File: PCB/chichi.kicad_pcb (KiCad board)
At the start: 2 copper layers, 59 x 53 mm, 6 parts, among them U1 ESP32-C3_SUPERMINI_TH, U2 Charger_Module

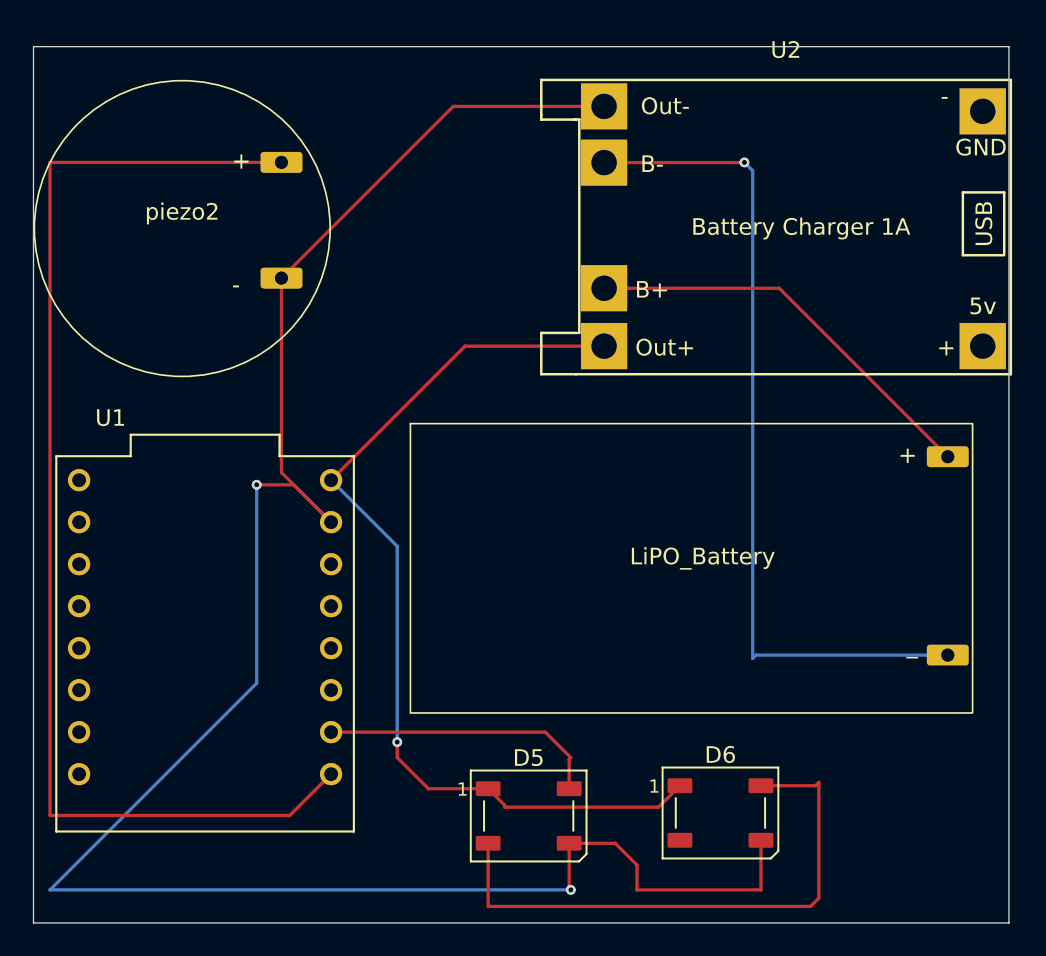
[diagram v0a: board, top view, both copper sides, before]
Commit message: Add MT3608 Module
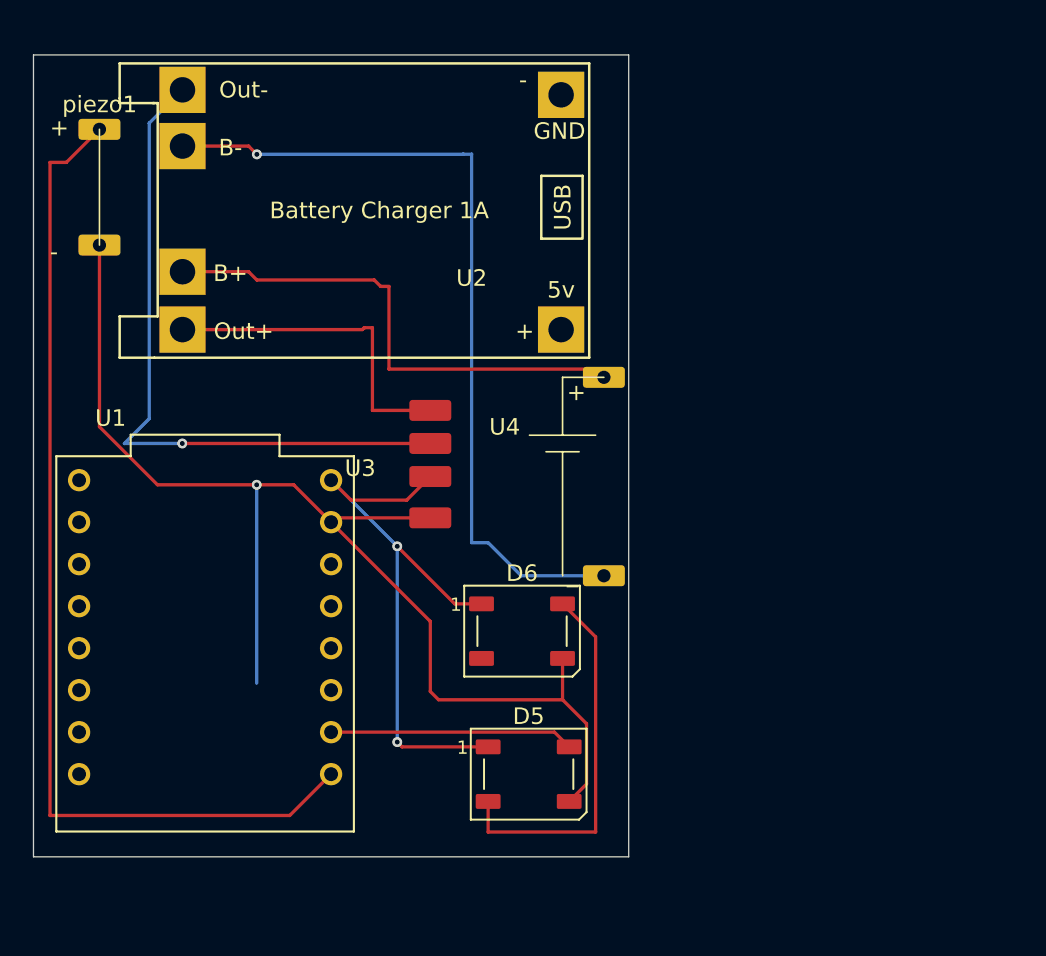
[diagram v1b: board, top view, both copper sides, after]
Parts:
- removed LiPO_Battery: ~, charger:LiPo
- removed piezo2: ~, charger:piezo
- added U3: ~, charger:LiPo, F.Cu at (168.5, 94.5)
- added U4: MT3608, charger:MT3608 Boost Converter, F.Cu at (178.0, 92.0)
- added piezo1: ~, charger:piezo, F.Cu at (147.5, 77.0)
- moved U2 25.5 mm to (183.1, 87.3)
- moved D6 16.3 mm to (179.1, 103.8)
- moved D5 2.53 mm to (179.4, 112.5)
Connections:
- U2 pad 3: Net-(D5-VDD) -> Net-(U2-OUT+)
- U2 pad 4: Net-(D5-VSS) -> Net-(U2-OUT-)
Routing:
- net Net-(D5-VSS): track 125.9 -> 75.8 mm, vias 2 -> 1
- net Net-(U2-OUT-): track 0.00 -> 41.5 mm, vias 0 -> 1
- net Net-(D5-VDD): track 57.3 -> 36.8 mm, vias 1 -> 2
- net Net-(U2-OUT+): track 0.00 -> 20.0 mm
- net Net-(D5-DOUT): track 34.6 -> 23.0 mm
- net Net-(U1-GPIO0): track 71.5 -> 61.4 mm
- net Net-(U2-B+): track 25.0 -> 31.1 mm
- net Net-(D5-DIN): track 17.1 -> 14.8 mm
- net Net-(U2-B-): track 50.6 -> 50.0 mm
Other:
- board size 59 x 53 mm -> 36 x 48.5 mm
